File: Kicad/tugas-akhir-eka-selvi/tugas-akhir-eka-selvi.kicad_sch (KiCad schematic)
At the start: 10 parts

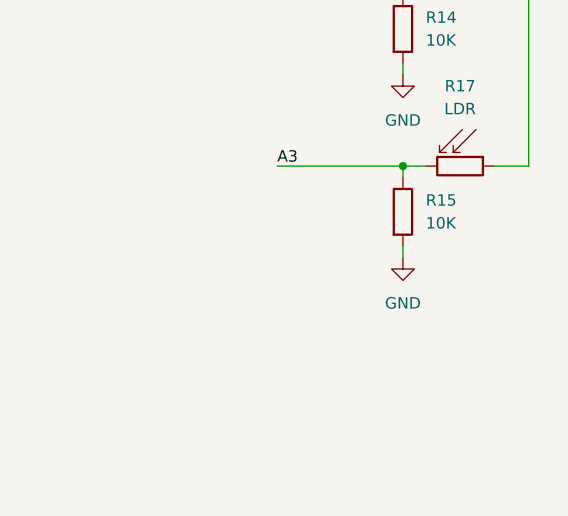
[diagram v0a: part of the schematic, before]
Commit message: Modif PCB LDR array
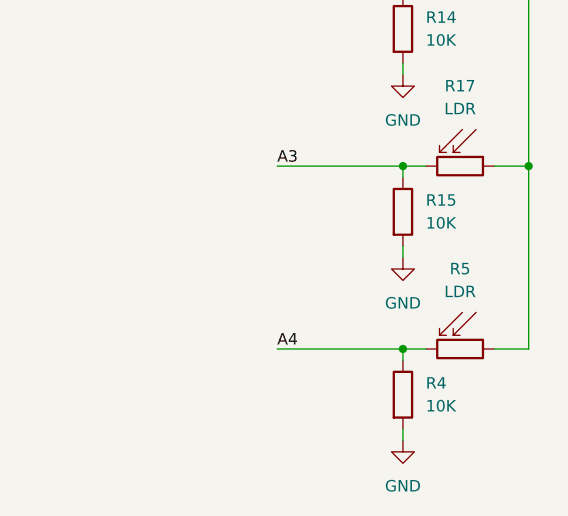
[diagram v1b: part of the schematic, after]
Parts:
- added R4: 10K, Resistor_THT:R_Axial_DIN0207_L6.3mm_D2.5mm_P10.16mm_Horizontal, symbol Device:R
- added R5: LDR, OptoDevice:R_LDR_4.9x4.2mm_P2.54mm_Vertical, symbol Sensor_Optical:A9060
- R1, R13, R16, R17, R3: footprint OptoDevice:R_LDR_5.0x4.1mm_P3mm_Vertical -> OptoDevice:R_LDR_4.9x4.2mm_P2.54mm_Vertical
- R11, R12, R14, R15, R2: footprint (none) -> Resistor_THT:R_Axial_DIN0207_L6.3mm_D2.5mm_P10.16mm_Horizontal
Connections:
- net +5V: now also R5.1
- net GND: now also R4.2
- new net A4: R4.1, R5.2

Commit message: Modif PCB
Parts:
- added J1: Conn_01x07, Connector_PinHeader_2.54mm:PinHeader_1x07_P2.54mm_Vertical, symbol Connector_Generic:Conn_01x07
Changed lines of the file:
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@@
+	)
+	(symbol
+		(lib_id "Connector_Generic:Conn_01x07")
+		(at 204.47 72.39 0)
+		(unit 1)
+		(exclude_from_sim no)
+		(in_bom yes)
+		(on_board yes)
+		(dnp no)
+		(fields_autoplaced yes)
+		(property "Reference" "J1"
+			(at 207.01 71.1199 0)
+			(effects
+				(font
+					(size 1.27 1.27)
+				)
+				(justify left)
+			)
+		)
+		(property "Value" "Conn_01x07"
+			(at 207.01 73.6599 0)
+			(effects
+				(font
+					(size 1.27 1.27)
+				)
+				(justify left)
+			)
+		)
+		(property "Footprint" "Connector_PinHeader_2.54mm:PinHeader_1x07_P2.54mm_Vertical"
+			(at 204.47 72.39 0)
+			(effects
+				(font
+					(size 1.27 1.27)
+				)
+				(hide yes)
+			)
+		)
+		(property "Datasheet" "~"
+			(at 204.47 72.39 0)
+			(effects
+				(font
+					(size 1.27 1.27)
+				)
+				(hide yes)
+			)
+		)
+		(property "Description" "Generic connector, single row, 01x07, script generated (kicad-library-utils/schlib/autogen/connector/)"
+			(at 204.47 72.39 0)
+			(effects
+				(font
+					(size 1.27 1.27)
+				)
+				(hide yes)
+			)
+		)
+		(pin "7"
+		)
+		(pin "5"
+		)
+		(pin "3"
+		)
+		(pin "6"
+		)
+		(pin "4"
+		)
+		(pin "2"
+		)
+		(pin "1"
+		)
+		(instances
+			(project "tugas-akhir-eka-selvi"
+				(path "/a7f2c55c-992a-456b-b57d-02001cd65dee"
+					(reference "J1")
+					(unit 1)
+				)
+			)
+		)
 	)
 	(symbol

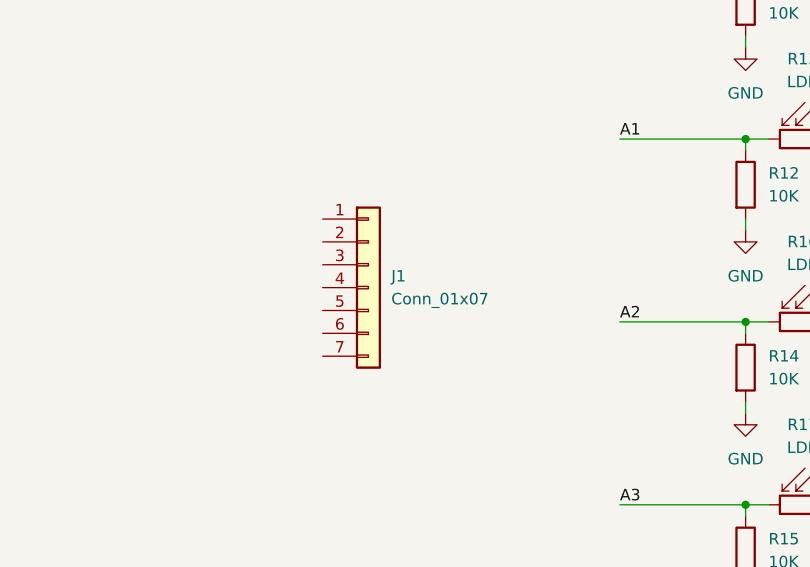
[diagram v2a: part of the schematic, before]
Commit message: Update array sensor schematic and PCB
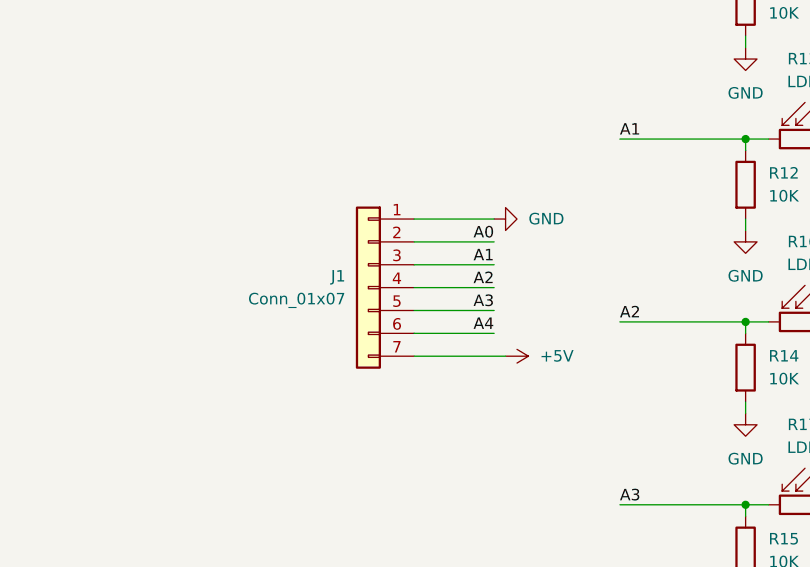
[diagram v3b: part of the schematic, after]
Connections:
- net +5V: now also J1.7 (Pin_7)
- net A0: now also J1.2 (Pin_2)
- net A1: now also J1.3 (Pin_3)
- net A2: now also J1.4 (Pin_4)
- net A3: now also J1.5 (Pin_5)
- net A4: now also J1.6 (Pin_6)
- net GND: now also J1.1 (Pin_1)
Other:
- moved on the sheet: J1
